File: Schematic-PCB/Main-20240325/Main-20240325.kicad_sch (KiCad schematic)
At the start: 17 parts, among them J1 Conn_01x20_Pin, J2 Conn_01x02_Pin, J3 Conn_01x03_Pin, J4 Conn_01x10_Pin, J5 Conn_02x05_Odd_Even, J6 Conn_01x15_Pin, U1 DEV-16771, U4 MOUDLE-SEEEDUINO-XIAO-ESP32C3

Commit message: 機体配線図などの追加
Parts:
- removed J2: Conn_01x02_Pin, symbol Connector:Conn_01x02_Pin
- added J2: Conn_01x03_Pin, symbol Connector:Conn_01x03_Pin
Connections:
- net +3.3V: now also J2.2 (Pin_2)
- net +5V: now also J2.1 (Pin_1)
- net GND: now also J2.3 (Pin_3)
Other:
- moved on the sheet: C1
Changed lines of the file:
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@@
 	(wire
 		(pts
-			(xy 72.39 163.83) (xy 67.31 163.83)
+			(xy 77.47 163.83) (xy 67.31 163.83)
 		)
 		(stroke
@@
 	(wire
 		(pts
+			(xy 67.31 161.29) (xy 72.39 161.29)
+		)
+		(stroke
+			(width 0)
+			(type default)
+		)
+	)
+	(wire
+		(pts
 			(xy 54.61 96.52) (xy 57.15 96.52)
 		)
@@
 	(wire
 		(pts
-			(xy 82.55 168.91) (xy 82.55 171.45)
+			(xy 86.36 168.91) (xy 86.36 171.45)
 		)
 		(stroke
@@
 	(wire
 		(pts
+			(xy 72.39 158.75) (xy 72.39 161.29)
+		)
+		(stroke
+			(width 0)
+			(type default)
+		)
+	)
+	(wire
+		(pts
 			(xy -10.16 81.28) (xy -10.16 78.74)
 		)
@@
 	(wire
 		(pts
-			(xy 72.39 158.75) (xy 72.39 163.83)
+			(xy 77.47 158.75) (xy 77.47 163.83)
 		)
 		(stroke
@@
 	(wire
 		(pts
-			(xy 82.55 158.75) (xy 82.55 161.29)
+			(xy 86.36 158.75) (xy 86.36 161.29)
 		)
 		(stroke
@@
 	)
 	(symbol
+		(lib_id "power:+5V")
+		(at 72.39 158.75 0)
+		(unit 1)
+		(exclude_from_sim no)
+		(in_bom yes)
+		(on_board yes)
+		(dnp no)
+		(fields_autoplaced yes)
+		(property "Reference" "#PWR025"
+			(at 72.39 162.56 0)
+			(effects
+				(font
+					(size 1.27 1.27)
+				)
+				(hide yes)
+			)
+		)
+		(property "Value" "+5V"
+			(at 72.39 153.67 0)
+			(effects
+				(font
+					(size 1.27 1.27)
+				)
+			)
+		)
+		(property "Footprint" ""
+			(at 72.39 158.75 0)
+			(effects
+				(font
+					(size 1.27 1.27)
+				)
+				(hide yes)
+			)
+		)
+		(property "Datasheet" ""
+			(at 72.39 158.75 0)
+			(effects
+				(font
+					(size 1.27 1.27)
+				)
+				(hide yes)
+			)
+		)
+		(property "Description" "Power symbol creates a global label with name \"+5V\""
+			(at 72.39 158.75 0)
+			(effects
+				(font
+					(size 1.27 1.27)
+				)
+				(hide yes)
+			)
+		)
+		(pin "1"
+		)
+		(instances
+			(project "Main-20240325"
+				(path "/d42c2da0-c5d1-4e9e-abe5-6ac5f9ded35c"
+					(reference "#PWR025")
+					(unit 1)
+				)
+			)
+		)
+	)
+	(symbol
 		(lib_id "power:GND")
 		(at -81.28 54.61 0)
@@
 	(symbol
 		(lib_id "power:GND")
-		(at 82.55 171.45 0)
+		(at 86.36 171.45 0)
 		(unit 1)
 		(exclude_from_sim no)
@@
 		(fields_autoplaced yes)
 		(property "Reference" "#PWR010"
-			(at 82.55 177.8 0)
+			(at 86.36 177.8 0)
 			(effects
 				(font
@@
 		)
 		(property "Value" "GND"
-			(at 82.55 176.53 0)
+			(at 86.36 176.53 0)
 			(effects
 				(font
@@
 		)
 		(property "Footprint" ""
-			(at 82.55 171.45 0)
+			(at 86.36 171.45 0)
 			(effects
 				(font
@@
 		)
 		(property "Datasheet" ""
-			(at 82.55 171.45 0)
+			(at 86.36 171.45 0)
 			(effects
 				(font
@@
 		)
 		(property "Description" ""
-			(at 82.55 171.45 0)
+			(at 86.36 171.45 0)
 			(effects
 				(font
@@
 	(symbol
 		(lib_id "Device:C")
-		(at 82.55 165.1 0)
+		(at 86.36 165.1 0)
 		(unit 1)
 		(exclude_from_sim no)
@@
 		(fields_autoplaced yes)
 		(property "Reference" "C1"
-			(at 86.36 163.83 0)
+			(at 90.17 163.83 0)
 			(effects
 				(font
@@
 		)
 		(property "Value" "C"
-			(at 86.36 166.37 0)
+			(at 90.17 166.37 0)
 			(effects
 				(font
@@
 		)
 		(property "Footprint" ""
-			(at 83.5152 168.91 0)
+			(at 87.3252 168.91 0)
 			(effects
 				(font
@@
 		)
 		(property "Datasheet" "~"
-			(at 82.55 165.1 0)
+			(at 86.36 165.1 0)
 			(effects
 				(font
@@
 		)
 		(property "Description" ""
-			(at 82.55 165.1 0)
+			(at 86.36 165.1 0)
 			(effects
 				(font
@@
 	)
 	(symbol
-		(lib_id "Connector:Conn_01x02_Pin")
-		(at 62.23 163.83 0)
-		(unit 1)
-		(exclude_from_sim no)
-		(in_bom yes)
-		(on_board yes)
-		(dnp no)
-		(fields_autoplaced yes)
-		(property "Reference" "J2"
-			(at 62.865 158.75 0)
-			(effects
-				(font
-					(size 1.27 1.27)
-				)
-			)
-		)
-		(property "Value" "Conn_01x02_Pin"
-			(at 62.865 161.29 0)
-			(effects
-				(font
-					(size 1.27 1.27)
-				)
-			)
-		)
-		(property "Footprint" ""
-			(at 62.23 163.83 0)
-			(effects
-				(font
-					(size 1.27 1.27)
-				)
-				(hide yes)
-			)
-		)
-		(property "Datasheet" "~"
-			(at 62.23 163.83 0)
-			(effects
-				(font
-					(size 1.27 1.27)
-				)
-				(hide yes)
-			)
-		)
-		(property "Description" ""
-			(at 62.23 163.83 0)
-			(effects
-				(font
-					(size 1.27 1.27)
-				)
-				(hide yes)
-			)
-		)
-		(pin "1"
-		)
-		(pin "2"
-		)
-		(instances
-			(project "Main-20240325"
-				(path "/d42c2da0-c5d1-4e9e-abe5-6ac5f9ded35c"
-					(reference "J2")
-					(unit 1)
-				)
-			)
-		)
-	)
-	(symbol
 		(lib_id "@MyLibrary:MOUDLE-SEEEDUINO-XIAO-ESP32C3")
 		(at 172.72 92.71 0)
@@
 	)
 	(symbol
+		(lib_id "Connector:Conn_01x03_Pin")
+		(at 62.23 163.83 0)
+		(unit 1)
+		(exclude_from_sim no)
+		(in_bom yes)
+		(on_board yes)
+		(dnp no)
+		(fields_autoplaced yes)
+		(property "Reference" "J2"
+			(at 62.865 156.21 0)
+			(effects
+				(font
+					(size 1.27 1.27)
+				)
+			)
+		)
+		(property "Value" "Conn_01x03_Pin"
+			(at 62.865 158.75 0)
+			(effects
+				(font
+					(size 1.27 1.27)
+				)
+			)
+		)
+		(property "Footprint" ""
+			(at 62.23 163.83 0)
+			(effects
+				(font
+					(size 1.27 1.27)
+				)
+				(hide yes)
+			)
+		)
+		(property "Datasheet" "~"
+			(at 62.23 163.83 0)
+			(effects
+				(font
+					(size 1.27 1.27)
+				)
+				(hide yes)
+			)
+		)
+		(property "Description" "Generic connector, single row, 01x03, script generated"
+			(at 62.23 163.83 0)
+			(effects
+				(font
+					(size 1.27 1.27)
+				)
+				(hide yes)
+			)
+		)
+		(pin "1"
+		)
+		(pin "3"
+		)
+		(pin "2"
+		)
+		(instances
+			(project "Main-20240325"
+				(path "/d42c2da0-c5d1-4e9e-abe5-6ac5f9ded35c"
+					(reference "J2")
+					(unit 1)
+				)
+			)
+		)
+	)
+	(symbol
 		(lib_id "power:GND")
 		(at 105.41 134.62 0)
@@
 	(symbol
 		(lib_id "power:+3.3V")
-		(at 72.39 158.75 0)
+		(at 77.47 158.75 0)
 		(unit 1)
 		(exclude_from_sim no)
@@
 		(fields_autoplaced yes)
 		(property "Reference" "#PWR06"
-			(at 72.39 162.56 0)
+			(at 77.47 162.56 0)
 			(effects
 				(font
@@
 		)
 		(property "Value" "+3.3V"
-			(at 72.39 153.67 0)
+			(at 77.47 153.67 0)
 			(effects
 				(font
@@
 		)
 		(property "Footprint" ""
-			(at 72.39 158.75 0)
+			(at 77.47 158.75 0)
 			(effects
 				(font
@@
 		)
 		(property "Datasheet" ""
-			(at 72.39 158.75 0)
+			(at 77.47 158.75 0)
 			(effects
 				(font
@@
 		)
 		(property "Description" "Power symbol creates a global label with name \"+3.3V\""
-			(at 72.39 158.75 0)
+			(at 77.47 158.75 0)
 			(effects
 				(font
@@
 	(symbol
 		(lib_id "power:+3.3V")
-		(at 82.55 158.75 0)
+		(at 86.36 158.75 0)
 		(unit 1)
 		(exclude_from_sim no)
@@
 		(fields_autoplaced yes)
 		(property "Reference" "#PWR07"
-			(at 82.55 162.56 0)
+			(at 86.36 162.56 0)
 			(effects
 				(font
@@
 		)
 		(property "Value" "+3.3V"
-			(at 82.55 153.67 0)
+			(at 86.36 153.67 0)
 			(effects
 				(font
@@
 		)
 		(property "Footprint" ""
-			(at 82.55 158.75 0)
+			(at 86.36 158.75 0)
 			(effects
 				(font
@@
 		)
 		(property "Datasheet" ""
-			(at 82.55 158.75 0)
+			(at 86.36 158.75 0)
 			(effects
 				(font
@@
 		)
 		(property "Description" "Power symbol creates a global label with name \"+3.3V\""
-			(at 82.55 158.75 0)
+			(at 86.36 158.75 0)
 			(effects
 				(font

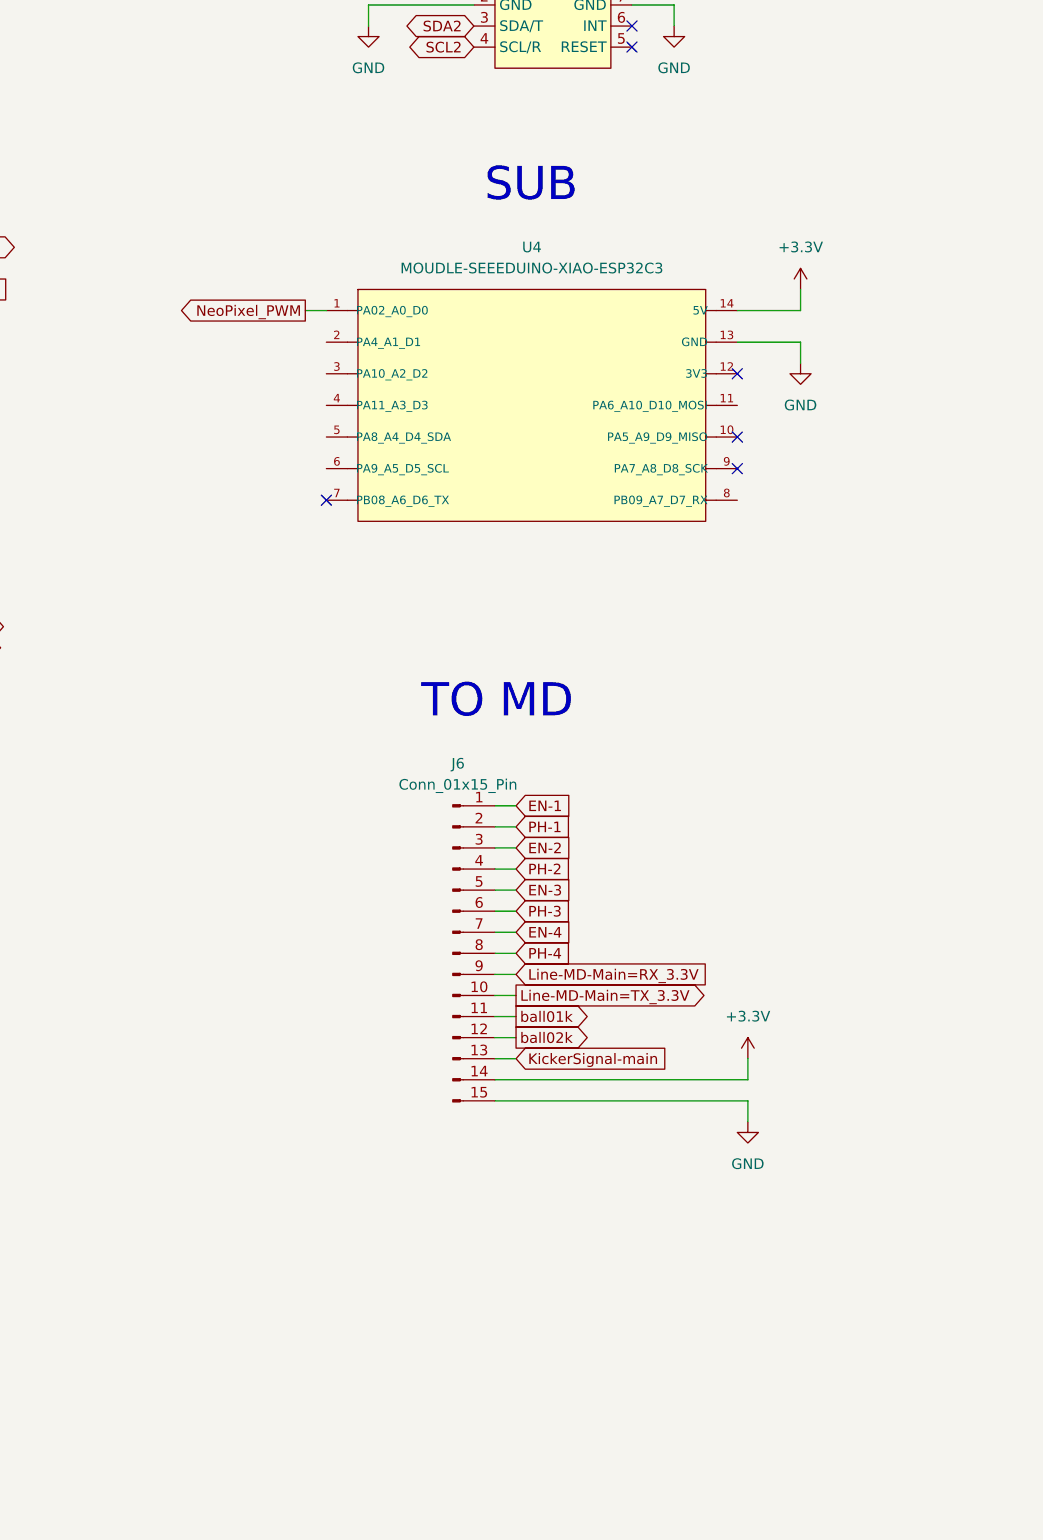
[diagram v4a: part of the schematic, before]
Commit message: メイン基板の回路図を修正しました
ESP32C3の使用禁止ピンなどの修正
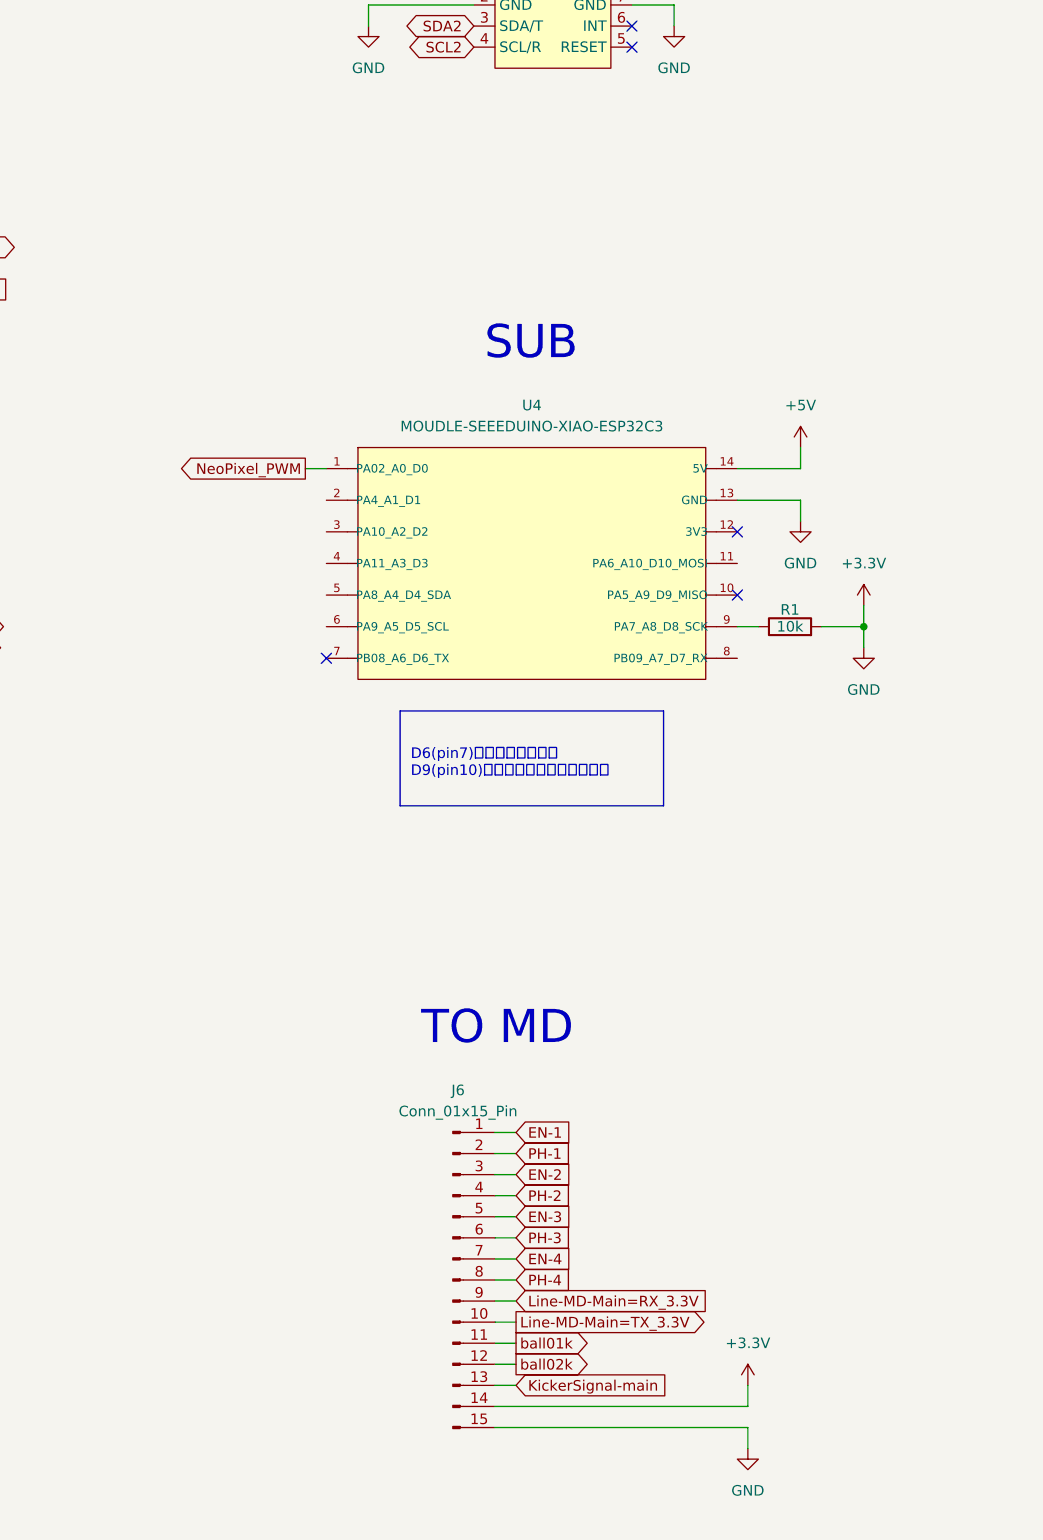
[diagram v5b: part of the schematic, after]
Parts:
- added R1: 10k, symbol Device:R
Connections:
- net GND is gone; now on net +3.3V: C1.2, D1.1 (K), D2.1 (K), D3.1 (K), J1.19 (Pin_19), J1.20 (Pin_20), J2.3 (Pin_3), J3.3 (Pin_3), J4.2 (Pin_2), J5.6 (Pin_6), J6.15 (Pin_15), U1.GND1 (GND), U1.GND2 (GND), U1.GND3 (GND), U1.GND4 (GND), U1.GND5 (GND), U2.2 (GND), U3.2 (GND), U3.7 (GND), U4.13 (GND)
- net +3.3V: now also R1.2; no longer U4.14 (5V)
- net +5V: now also U4.14 (5V)
- net at U4.9 (PA7_A8_D8_SCK): now also R1.1
- no-connect marks 17 -> 16
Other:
- note added: "D6(pin7)は基本使用しない D9(pin10)はスイッチ入力に使用する"
- moved on the sheet: J6, U4
